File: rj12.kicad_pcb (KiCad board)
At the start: 2 copper layers, 16 x 23 mm, 2 parts, among them J1 Conn_01x06, P1 RJ12_Housing

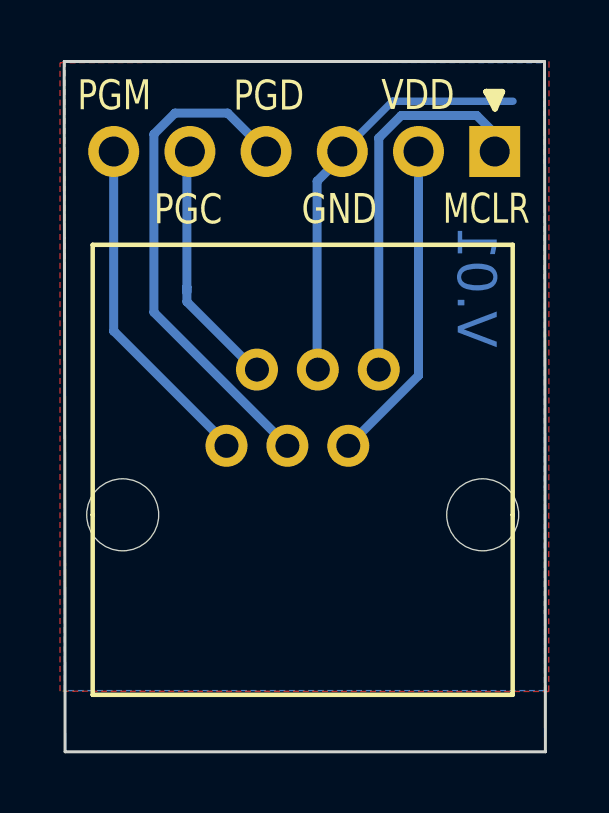
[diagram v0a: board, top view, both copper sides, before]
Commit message: Added copper poured with via stiching
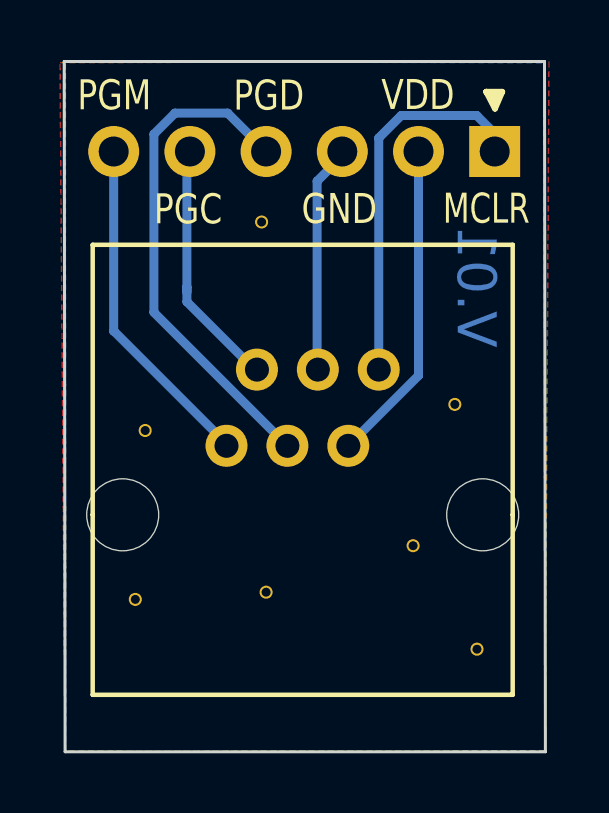
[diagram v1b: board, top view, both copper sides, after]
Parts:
- added REF**: Via(0.435-0.3mm), Via(0.435-0.3mm), F.Cu at (173.3, 119.1)
- added REF**: Via(0.435-0.3mm), Via(0.435-0.3mm), F.Cu at (166.1, 104.8)
- added REF**: Via(0.435-0.3mm), Via(0.435-0.3mm), F.Cu at (166.3, 117.2)
- added REF**: Via(0.435-0.3mm), Via(0.435-0.3mm), F.Cu at (161.9, 117.4)
- added REF**: Via(0.435-0.3mm), Via(0.435-0.3mm), F.Cu at (172.6, 110.9)
- added REF**: Via(0.435-0.3mm), Via(0.435-0.3mm), F.Cu at (162.2, 111.8)
- added REF**: Via(0.435-0.3mm), Via(0.435-0.3mm), F.Cu at (171.2, 115.6)
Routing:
- net pin3: track 14.1 -> 7.76 mm
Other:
- board text added: "ICD3 RJ-12 Connector"
- board text removed: "ICD3_Conn"
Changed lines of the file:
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@@
 (kicad_pcb (version 4) (host pcbnew 4.0.7)
   (general
-    (links 6)
+    (links 13)
     (no_connects 0)
-    (area 150.580402 95.879955 177.295 122.560001)
+    (area 159.489999 99.449999 175.630001 122.560001)
     (thickness 1.6)
     (drawings 34)
-    (tracks 29)
+    (tracks 27)
     (zones 0)
-    (modules 2)
+    (modules 9)
     (nets 7)
   )
@@
     (44 Edge.Cuts user)
     (45 Margin user)
-    (46 B.CrtYd user)
-    (47 F.CrtYd user)
-    (48 B.Fab user)
-    (49 F.Fab user)
+    (46 B.CrtYd user hide)
+    (47 F.CrtYd user hide)
+    (48 B.Fab user hide)
+    (49 F.Fab user hide)
   )
   (setup
@@
     (mod_text_size 1 1)
     (mod_text_width 0.15)
-    (pad_size 1.4 1.4)
-    (pad_drill 0.8)
+    (pad_size 0.435 0.435)
+    (pad_drill 0.3)
     (pad_to_mask_clearance 0)
     (aux_axis_origin 159.54 99.5)
     (grid_origin 159.54 99.5)
-    (visible_elements 7FFFFFFF)
+    (visible_elements 7FFFFF7F)
     (pcbplotparams
       (layerselection 0x0ffff_80000001)
@@
     (add_net pin6)
   )
+  (module "Via(0.435-0.3mm)" (layer F.Cu)
+    (at 173.3 119.09)
+    (fp_text reference REF** (at 0.46 1.67) (layer F.SilkS) hide
+      (effects (font (size 1 1) (thickness 0.15)))
+    )
+    (fp_text value "Via(0.435-0.3mm)" (at -0.07 -1.65) (layer F.Fab) hide
+      (effects (font (size 1 1) (thickness 0.15)))
+    )
+    (pad 1 thru_hole circle (at 0 0) (size 0.435 0.435) (drill 0.3) (layers *.Cu)
+      (net 3 pin3) (zone_connect 2))
+  )
+  (module "Via(0.435-0.3mm)" (layer F.Cu)
+    (at 166.12 104.85)
+    (fp_text reference REF** (at 0.46 1.67) (layer F.SilkS) hide
+      (effects (font (size 1 1) (thickness 0.15)))
+    )
+    (fp_text value "Via(0.435-0.3mm)" (at -0.07 -1.65) (layer F.Fab) hide
+      (effects (font (size 1 1) (thickness 0.15)))
+    )
+    (pad 1 thru_hole circle (at 0 0) (size 0.435 0.435) (drill 0.3) (layers *.Cu)
+      (net 3 pin3) (zone_connect 2))
+  )
+  (module "Via(0.435-0.3mm)" (layer F.Cu)
+    (at 166.27 117.19)
+    (fp_text reference REF** (at 0.46 1.67) (layer F.SilkS) hide
+      (effects (font (size 1 1) (thickness 0.15)))
+    )
+    (fp_text value "Via(0.435-0.3mm)" (at -0.07 -1.65) (layer F.Fab) hide
+      (effects (font (size 1 1) (thickness 0.15)))
+    )
+    (pad 1 thru_hole circle (at 0 0) (size 0.435 0.435) (drill 0.3) (layers *.Cu)
+      (net 3 pin3) (zone_connect 2))
+  )
+  (module "Via(0.435-0.3mm)" (layer F.Cu)
+    (at 161.91 117.43)
+    (fp_text reference REF** (at 0.46 1.67) (layer F.SilkS) hide
+      (effects (font (size 1 1) (thickness 0.15)))
+    )
+    (fp_text value "Via(0.435-0.3mm)" (at -0.07 -1.65) (layer F.Fab) hide
+      (effects (font (size 1 1) (thickness 0.15)))
+    )
+    (pad 1 thru_hole circle (at 0 0) (size 0.435 0.435) (drill 0.3) (layers *.Cu)
+      (net 3 pin3) (zone_connect 2))
+  )
+  (module "Via(0.435-0.3mm)" (layer F.Cu)
+    (at 172.56 110.93)
+    (fp_text reference REF** (at 0.46 1.67) (layer F.SilkS) hide
+      (effects (font (size 1 1) (thickness 0.15)))
+    )
+    (fp_text value "Via(0.435-0.3mm)" (at -0.07 -1.65) (layer F.Fab) hide
+      (effects (font (size 1 1) (thickness 0.15)))
+    )
+    (pad 1 thru_hole circle (at 0 0) (size 0.435 0.435) (drill 0.3) (layers *.Cu)
+      (net 3 pin3) (zone_connect 2))
+  )
+  (module "Via(0.435-0.3mm)" (layer F.Cu)
+    (at 162.24 111.8)
+    (fp_text reference REF** (at 0.46 1.67) (layer F.SilkS) hide
+      (effects (font (size 1 1) (thickness 0.15)))
+    )
+    (fp_text value "Via(0.435-0.3mm)" (at -0.07 -1.65) (layer F.Fab) hide
+      (effects (font (size 1 1) (thickness 0.15)))
+    )
+    (pad 1 thru_hole circle (at 0 0) (size 0.435 0.435) (drill 0.3) (layers *.Cu)
+      (net 3 pin3) (zone_connect 2))
+  )
+  (module "Via(0.435-0.3mm)" (layer F.Cu)
+    (at 171.17 115.64)
+    (fp_text reference REF** (at 0.46 1.67) (layer F.SilkS) hide
+      (effects (font (size 1 1) (thickness 0.15)))
+    )
+    (fp_text value "Via(0.435-0.3mm)" (at -0.07 -1.65) (layer F.Fab) hide
+      (effects (font (size 1 1) (thickness 0.15)))
+    )
+    (pad 1 thru_hole circle (at 0 0) (size 0.435 0.435) (drill 0.3) (layers *.Cu)
+      (net 3 pin3) (zone_connect 2))
+  )
   (module RJ12-Housing:RJ12 (layer F.Cu)
     (at 165.19 113.42)
@@
   (gr_line (start 173.61 100.51) (end 174.14 100.51) (layer F.SilkS) (width 0.2))
   (gr_line (start 175.55 99.5) (end 175.58 122.51) (layer Edge.Cuts) (width 0.1))
-  (gr_line (start 166.59 116.81) (end 165.91 117.33) (layer B.SilkS) (width 0.2))
-  (gr_line (start 166.41 116.54) (end 165.65 116.64) (layer B.SilkS) (width 0.2))
-  (gr_line (start 166.35 116.25) (end 165.65 116.04) (layer B.SilkS) (width 0.2))
-  (gr_line (start 168.57 116.76) (end 169.17 117.33) (layer B.SilkS) (width 0.2))
-  (gr_line (start 168.72 116.5) (end 169.61 116.58) (layer B.SilkS) (width 0.2))
-  (gr_line (start 168.75 116.17) (end 169.59 115.88) (layer B.SilkS) (width 0.2))
-  (gr_line (start 167.28 116.96) (end 167.84 116.43) (layer B.SilkS) (width 0.2))
-  (gr_line (start 167.14 116.46) (end 167.93 116.97) (layer B.SilkS) (width 0.2))
-  (gr_circle (center 168.1 115.86) (end 168.2 115.8) (layer B.SilkS) (width 0.2))
-  (gr_circle (center 167.02 115.87) (end 167.12 115.81) (layer B.SilkS) (width 0.2))
-  (gr_line (start 166.17 114.3) (end 166.31 115.43) (layer B.SilkS) (width 0.2))
-  (gr_line (start 166.81 114.87) (end 166.17 114.3) (layer B.SilkS) (width 0.2))
-  (gr_line (start 168.88 114.26) (end 168.71 115.16) (layer B.SilkS) (width 0.2))
-  (gr_line (start 168.18 114.75) (end 168.88 114.26) (layer B.SilkS) (width 0.2))
-  (gr_circle (center 167.573887 116.12) (end 168.443887 114.99) (layer B.SilkS) (width 0.2))
+  (gr_line (start 166.3 116.11) (end 165.62 116.63) (layer B.SilkS) (width 0.2))
+  (gr_line (start 166.12 115.84) (end 165.36 115.94) (layer B.SilkS) (width 0.2))
+  (gr_line (start 166.06 115.55) (end 165.36 115.34) (layer B.SilkS) (width 0.2))
+  (gr_line (start 168.28 116.06) (end 168.88 116.63) (layer B.SilkS) (width 0.2))
+  (gr_line (start 168.43 115.8) (end 169.32 115.88) (layer B.SilkS) (width 0.2))
+  (gr_line (start 168.46 115.47) (end 169.3 115.18) (layer B.SilkS) (width 0.2))
+  (gr_line (start 166.99 116.26) (end 167.55 115.73) (layer B.SilkS) (width 0.2))
+  (gr_line (start 166.85 115.76) (end 167.64 116.27) (layer B.SilkS) (width 0.2))
+  (gr_circle (center 167.81 115.16) (end 167.91 115.1) (layer B.SilkS) (width 0.2))
+  (gr_circle (center 166.73 115.17) (end 166.83 115.11) (layer B.SilkS) (width 0.2))
+  (gr_line (start 165.88 113.6) (end 166.02 114.73) (layer B.SilkS) (width 0.2))
+  (gr_line (start 166.52 114.17) (end 165.88 113.6) (layer B.SilkS) (width 0.2))
+  (gr_line (start 168.59 113.56) (end 168.42 114.46) (layer B.SilkS) (width 0.2))
+  (gr_line (start 167.89 114.05) (end 168.59 113.56) (layer B.SilkS) (width 0.2))
+  (gr_circle (center 167.283887 115.42) (end 168.153887 114.29) (layer B.SilkS) (width 0.2))
   (gr_line (start 173.95 100.67) (end 173.9 100.76) (layer F.SilkS) (width 0.2))
   (gr_line (start 173.61 100.51) (end 173.95 100.67) (layer F.SilkS) (width 0.2))
   (gr_line (start 173.9 101.07) (end 173.61 100.51) (layer F.SilkS) (width 0.2))
-  (gr_text ICD3_Conn (at 167.6 118.77) (layer B.SilkS)
+  (gr_text "ICD3 RJ-12\nConnector" (at 167.35 119.26) (layer B.SilkS)
     (effects (font (size 1 1) (thickness 0.25)) (justify mirror))
   )
@@
   (segment (start 171.35 109.97) (end 169.01 112.31) (width 0.3) (layer B.Cu) (net 2))
   (segment (start 171.5 102.5) (end 171.3 102.7) (width 0.3) (layer B.Cu) (net 2))
-  (segment (start 168.81 102.5) (end 170.485011 100.824989) (width 0.25) (layer B.Cu) (net 3))
-  (segment (start 170.485011 100.824989) (end 174.499991 100.824989) (width 0.25) (layer B.Cu) (net 3))
   (segment (start 168.96 102.5) (end 167.970005 103.489995) (width 0.3) (layer B.Cu) (net 3))
   (segment (start 167.970005 103.489995) (end 167.970005 109.745005) (width 0.3) (layer B.Cu) (net 3))
@@
     (polygon
       (pts
-        (xy 159.4 99.54) (xy 175.7 99.5) (xy 175.69 120.5) (xy 159.4 120.49)
+        (xy 159.4 99.54) (xy 175.7 99.5) (xy 175.57 122.47) (xy 159.57 122.51)
       )
     )
@@
     (polygon
       (pts
-        (xy 159.58 99.51) (xy 175.53 99.54) (xy 175.55 120.47) (xy 159.54 120.47)
+        (xy 159.58 99.51) (xy 175.53 99.54) (xy 175.57 122.51) (xy 159.59 122.49)
       )
     )
